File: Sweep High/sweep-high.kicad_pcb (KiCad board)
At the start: 2 copper layers, 229.8 x 95.2 mm, 55 parts, among them J1 AudioJack4dpb, J2 AudioJack4dpb, SW10 SW_Push, SW11 SW_Push, SW11_r1 SW_Push, SW12 SW_Push, SW12_r1 SW_Push, SW13_r1 SW_Push, SW14 SW_Push, SW15 SW_Push, SW15_r1 SW_Push, SW16 SW_Push, SW16_r1 SW_Push, SW17 SW_Push, SW17_r1 SW_Push, SW18 SW_Push, SW18_r1 SW_Push, SW2 SW_Push, SW2 SW_SPDT, SW20 SW_Push, SW20_r1 SW_Push, SW21 SW_Push, SW21_r1 SW_Push, SW2_r1 SW_Push, SW3 SW_Push, SW3_r1 SW_Push, SW4 SW_Push, SW4_r1 SW_Push, SW5 SW_Push, SW5_r1 SW_Push, SW6 SW_Push, SW6_r1 SW_Push, SW7_r1 SW_Push, SW8 SW_Push, SW8_r1 SW_Push, SW9 SW_Push, SW9_r1 SW_Push, U1 ProMicro-kbd, U2 ProMicro-kbd

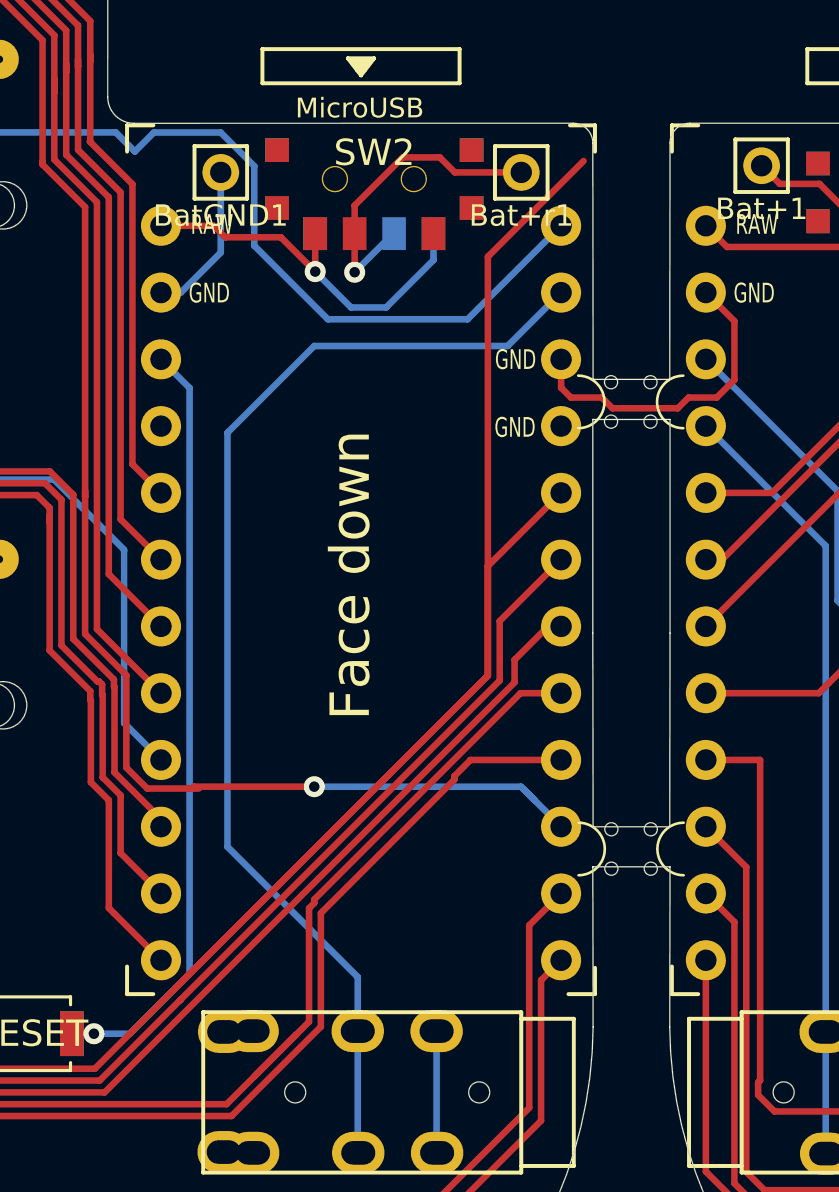
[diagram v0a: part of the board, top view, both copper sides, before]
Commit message: fix vcc tidy up routing
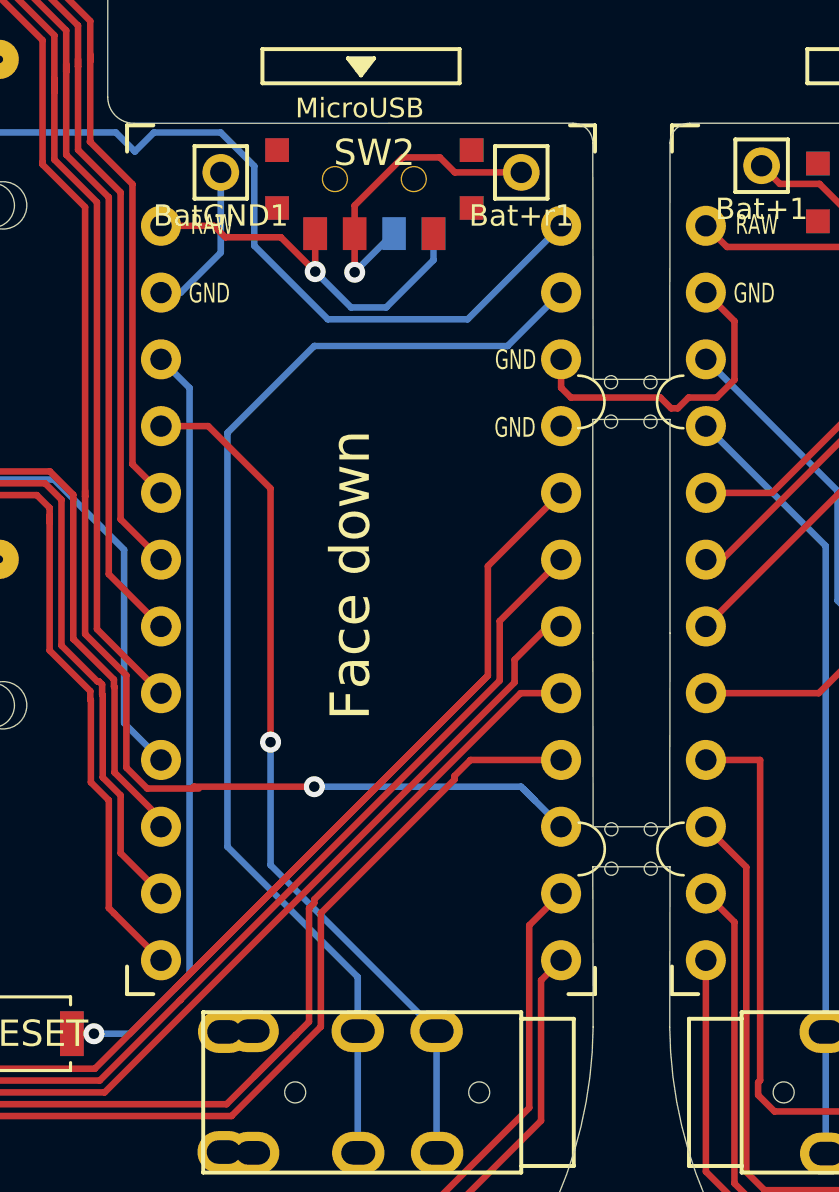
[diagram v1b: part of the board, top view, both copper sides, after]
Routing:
- net vcc: track 34.2 -> 62.7 mm, vias 0 -> 1
- net Switch11: track 199.5 -> 178.4 mm
